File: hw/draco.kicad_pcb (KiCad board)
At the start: 4 copper layers, 47.5 x 62 mm, 172 parts, among them P1 CONN_13X3, P10 MICROSD, P11 CONN_9, P12 CONN_2, P13 CONN_6, P14 CONN_2, P18 CONN_1, P19 CONN_1, P2 CONN_4, P20 CONN_1, P21 CONN_1, P22 CONN_1, P3 CONN_4, P4 MICROUSB, P5 CONN_4, P6 CONN_6, P7 CONN_4, P8 CONN_4, P9 CONN_4, Q1 NTA4153NT1G, Q2 NTA4153NT1G, Q3 NTA4151PT1G, Q4 PDTC114EE, Q5 PDTC114EE, Q6 PDTC114EE, Q7 PDTC114EE, SW1 STG719, SW2 EVQP7A01K, U1 XBEE, U10 FLASH-SPI-SO8, U12 MAX4090, U13 MPU-9250, U2 LTC4411, U3 SN65HVD233, U4 ADP3338AKCZ-3.3, U5 LT1761-3.3, U6 EL1883, U7 STM32F427VIT6, U8 STM32F303CC, U9 MS5611, X1 8MHz, X2 8MHz

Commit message: hw: added diode from servo +5V to +3.3V stabs, TSV protection diode
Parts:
- added D10: 1SMB7.0AT3G, do214aa_dandys, B.Cu at (232.9, 198.1)
- added D9: MBRS130T3G, do214aa_dandys, B.Cu at (203.7, 188.9)
- R70: value 220R -> 390R
- U10: value FLASH-SPI-SO8 -> MICRON N25Q032A13ESC40G
- moved G4 0.38 mm to (226.5, 191.0)
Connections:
- C2 pad 1: +5V -> N-00000153
- D1 pad 2: +5V -> N-00000153
- L1 pad 1: +5V -> N-00000153
- U2 pad 5: +5V -> N-00000153
- U4 pad IN: +5V -> N-00000153
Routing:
- net N-00000153: track 0.00 -> 93.3 mm, vias 0 -> 4
- net +5V: track 240.8 -> 224.9 mm, vias 9 -> 8
- net F4_NRST: track 54.1 -> 55.1 mm
- net GND: track 211.4 -> 210.7 mm, vias 58 -> 59
- net +3.3V: track 145.1 -> 144.5 mm

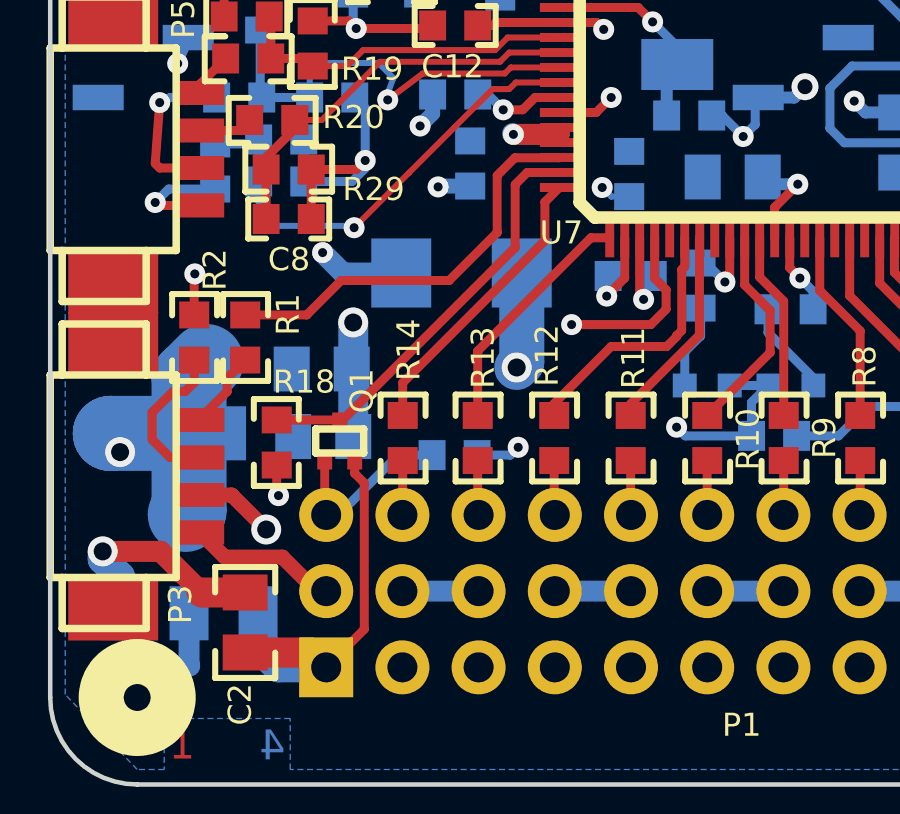
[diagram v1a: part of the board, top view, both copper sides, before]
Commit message: hw: SBUS inverting FET replaced by XOR gate (controllable inverter)
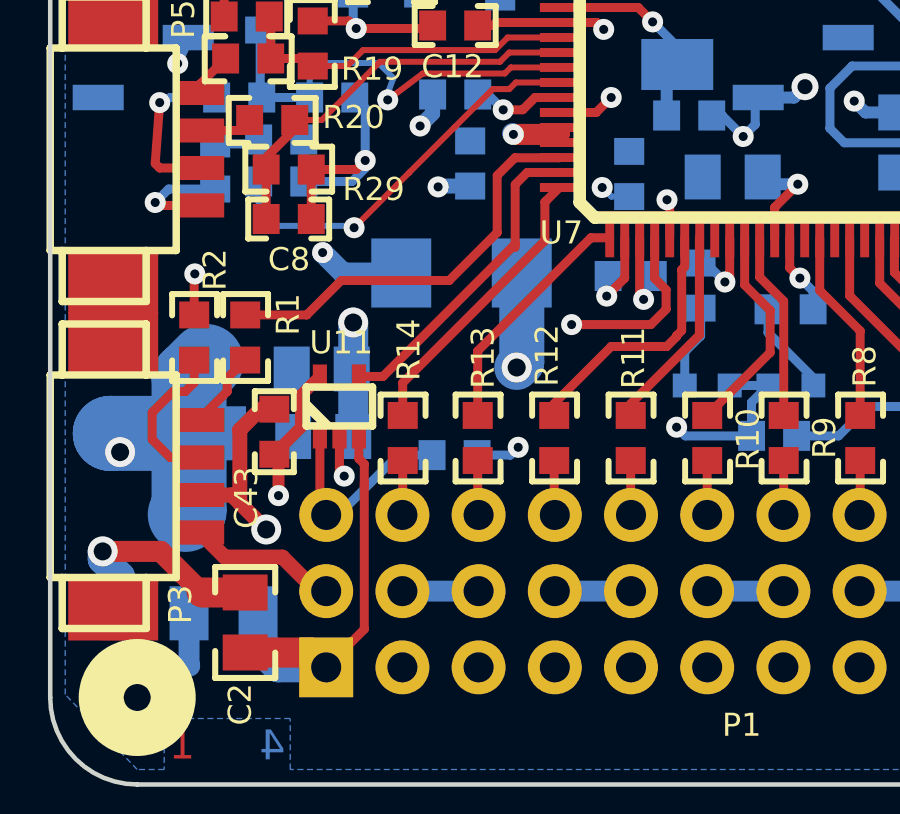
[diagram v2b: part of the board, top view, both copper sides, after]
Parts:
- removed Q1: NTA4153NT1G, sc75
- removed R18: 4k7, r_0603
- added C43: 100nF, c_0603, F.Cu at (197.5, 194.2)
- added U11: SN74AHC1G86, sot323-5_2, F.Cu at (199.6, 193.4)
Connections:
- U7 pad 30: (no net) -> SBUS_UART_INVERT
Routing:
- net SBUS_UART_INVERT: track 0.00 -> 21.4 mm, vias 0 -> 2
- net GND: track 210.7 -> 215.5 mm
- net +3.3V: track 144.5 -> 148.2 mm
- net SBUS: track 14.1 -> 10.8 mm
- net N-00000149: track 6.19 -> 7.06 mm

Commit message: hw: added series resistor to USB VBUS sense pin
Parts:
- added R18: 39k, r_0603, F.Cu at (226.8, 178.9)
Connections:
- D1 pad 1: USBVB -> N-00000167
- P4 pad 1: USBVB -> N-00000167
- U2 pad 1: USBVB -> N-00000167
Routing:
- net N-00000167: track 0.00 -> 19.7 mm, vias 0 -> 2
- net USBVB: track 21.5 -> 5.36 mm, vias 2 -> 0

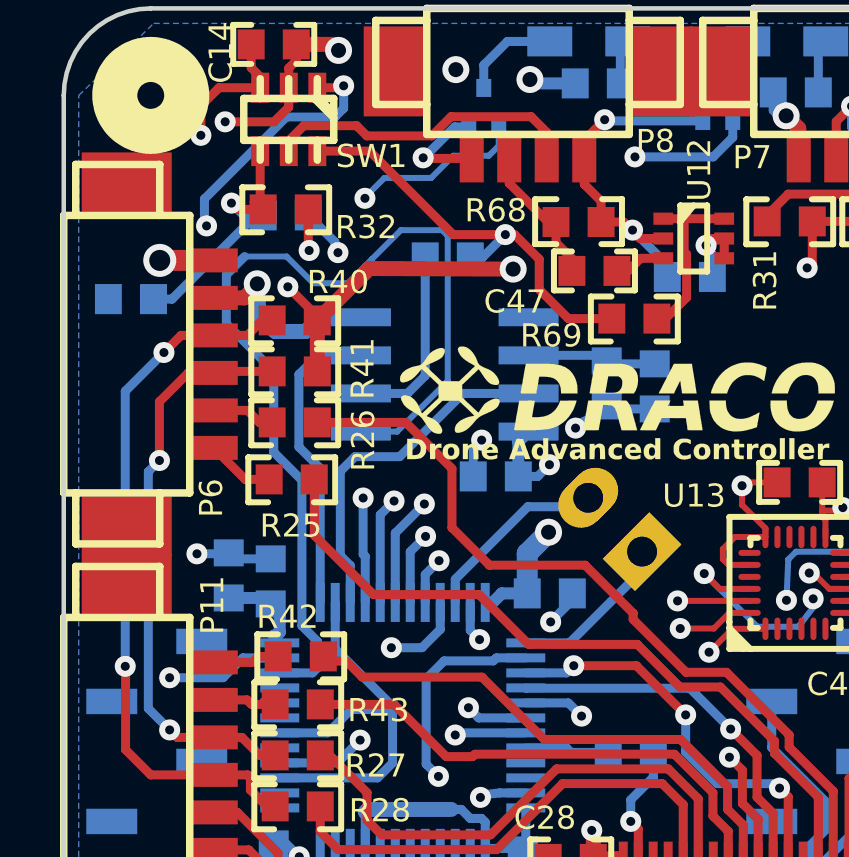
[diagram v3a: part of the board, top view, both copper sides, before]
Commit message: hw: add chroma filter to sync separator, removed unused CSYNC signal
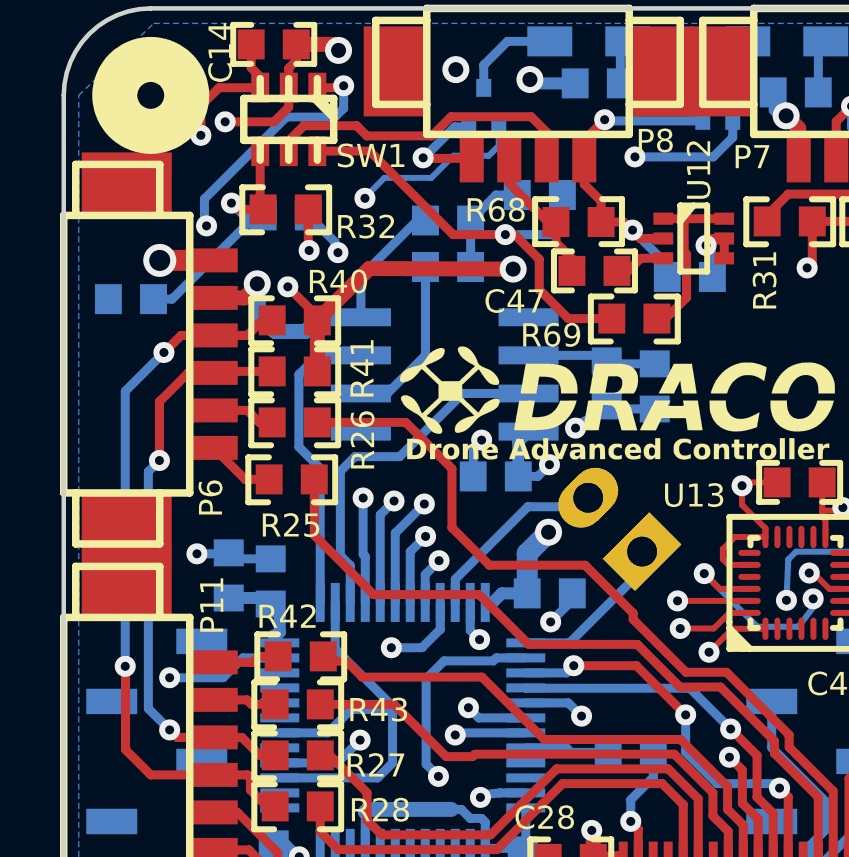
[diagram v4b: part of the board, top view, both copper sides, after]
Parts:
- added C44: 510pF, c_0603, B.Cu at (202.8, 151.1)
- added R71: 620R, r_0603, B.Cu at (205.9, 150.2)
- moved C15 0.32 mm to (202.8, 152.6)
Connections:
- C15 pad 1: N-00000150 (its old number) -> N-00000145
- R69 pad 1: N-00000150 (its old number) -> N-00000147
- SW1 pad 6: N-00000150 (its old number) -> N-00000147
- U6 pad 1: OSD_CSYNC -> (no net)
- U8 pad 22: OSD_CSYNC -> (no net)
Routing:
- net OSD_CSYNC: track 32.9 -> 0.00 mm
- net N-00000147: track 0.00 -> 15.7 mm, vias 0 -> 1
- net N-00000150 (its old number): track 14.2 -> 0.00 mm, vias 1 -> 0
- net GND: track 215.5 -> 219.7 mm
- net N-00000145: track 0.00 -> 3.46 mm
- net N-00000144: track 6.33 -> 5.62 mm
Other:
- board text added: "rev. 1.10 2014 by Dandys"
- board text removed: "rev. 1.00 2014 by Dandys"
